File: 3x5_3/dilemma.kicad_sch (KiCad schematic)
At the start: 248 parts, among them J1 USB_C_Receptacle_USB2.0, J102 NA_serial, J105 NA_Conn_01x04_Female, J113 Cirque, J3 NA_GC9A01, J4 Conn_01x05, J5 NA_Conn_01x02, J5001 USB_C_Receptacle_USB2.0, J5002 NA_Conn_01x02, J5003 NA_serial, J5004 NA_GC9A01, J5005 NA_Conn_01x04_Female, J5007 Cirque, J5008 Conn_01x05, J5009 Conn_01x05, J5010 Conn_01x05, SW1 SW_Push, SW101 NA_SW_Push, SW102 NA_SW_Push, SW103 NA_SW_Push, SW104 NA_SW_Push, SW105 NA_SW_Push, SW106 NA_SW_Push, SW107 NA_SW_Push, SW108 NA_SW_Push, SW109 NA_SW_Push, SW112 NA_SW_Push, SW113 NA_SW_Push, SW114 NA_SW_Push, SW115 NA_SW_Push, SW116 NA_SW_Push, SW117 NA_SW_Push, SW118 NA_SW_Push, SW119 NA_SW_Push, SW3001 NA_SW_Push, SW3002 NA_RotaryEncoder_Switch, SW5001 SW_Push, SW5002 NA_SW_Push, SW5003 NA_SW_Push, SW5004 NA_SW_Push, SW5005 NA_SW_Push, SW5006 NA_SW_Push, SW5007 NA_SW_Push, SW5008 NA_SW_Push, SW5009 NA_SW_Push, SW5010 NA_SW_Push, SW5011 NA_SW_Push, SW5012 NA_SW_Push, SW5013 NA_SW_Push, SW5014 NA_SW_Push, SW5015 NA_SW_Push, SW5016 NA_SW_Push, SW5017 NA_SW_Push, SW5018 NA_SW_Push, SW5019 NA_SW_Push, SW5020 NA_RotaryEncoder_Switch, SW5021 SW_SPST, SW5022 SW_SPST, U1 RP2040, U2 W25Q128JVS, U3 XC6210B332MR-G, U4 USBLC6-2P6, U5001 XC6210B332MR-G, U5002 RP2040, U5003 USBLC6-2P6, U5004 W25Q128JVS, U5005 USBLC6-2P6, U5006 USBLC6-2P6, Y1 Crystal_GND24, Y5001 Crystal_GND24

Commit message: add vik connector
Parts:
- added NA_JP5001, NA_JP5002, NA_JP5003, NA_JP5004: NA_Jumper_2_Open, local-libraries:SolderJumper-2_P1.3mm_Open_RoundedPad1.0x1.5mm, symbol Jumper:Jumper_2_Open
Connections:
- net QP_CS is gone; now on net VIK_GP1: J3.6 (~{CS}), U1.15 (GPIO12)
- net QP_CS_L is gone; now on net VIK_GP1_L: J5004.6 (~{CS}), U5002.15 (GPIO12)
- net QP_DC is gone; now on net VIK_GP2: J3.5 (D/C), U1.14 (GPIO11)
- net QP_DC_L is gone; now on net VIK_GP2_L: J5004.5 (D/C), U5002.14 (GPIO11)
- net +5V: now also NA_JP5004.1 (A)
- net +5V_L: now also NA_JP5003.1 (A)
- net at D5033.1 (DOUT): now also NA_JP5002.1 (A)
- net at D5051.1 (DOUT): now also NA_JP5001.1 (A)
- net VIK_GP2_L: now reaches J5007.4 (Pin_4)
- net VIK_GP1_L: now reaches J5007.6 (Pin_6)
- net at J5007.7 (Pin_7): now also NA_JP5003.2 (B)
- net VIK_RGB_L: now reaches J5007.8 (Pin_8)
- net VIK_RGB_L: now also NA_JP5001.2 (B)
- net VIK_GP2: now reaches J113.4 (Pin_4)
- net VIK_GP1: now reaches J113.6 (Pin_6)
- net at J113.7 (Pin_7): now also NA_JP5004.2 (B)
- net VIK_RGB: now reaches J113.8 (Pin_8)
- net VIK_RGB: now also NA_JP5002.2 (B)
- no-connect marks 30 -> 20
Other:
- moved on the sheet: C5001, C5002, C5003, C5004, C5005, C5006, C5007, C5008, C5009, C5010, C5011, C5012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

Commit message: DRC, leds
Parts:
- removed NA_JP5001, NA_JP5002: NA_Jumper_2_Open, local-libraries:SolderJumper-2_P1.3mm_Open_RoundedPad1.0x1.5mm, symbol Jumper:Jumper_2_Open
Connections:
- net VIK_RGB: now also D5033.1 (DOUT)
- net VIK_RGB_L: now also D5051.1 (DOUT)
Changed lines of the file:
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@@
 	(wire
 		(pts
+			(xy 628.65 76.2) (xy 638.81 76.2)
+		)
+		(stroke
+			(width 0)
+			(type default)
+		)
+	)
+	(wire
+		(pts
 			(xy 97.79 106.68) (xy 105.41 106.68)
 		)
@@
 	(wire
 		(pts
+			(xy 622.3 372.11) (xy 632.46 372.11)
+		)
+		(stroke
+			(width 0)
+			(type default)
+		)
+	)
+	(wire
+		(pts
 			(xy 455.93 359.41) (xy 473.71 359.41)
 		)
@@
 	)
 	(symbol
-		(lib_id "Jumper:Jumper_2_Open")
-		(at 633.73 76.2 0)
-		(unit 1)
-		(exclude_from_sim no)
-		(in_bom no)
-		(on_board yes)
-		(dnp no)
-		(property "Reference" "NA_JP5002"
-			(at 632.714 72.898 0)
-			(effects
-				(font
-					(size 1.27 1.27)
-				)
-			)
-		)
-		(property "Value" "NA_Jumper_2_Open"
-			(at 642.112 69.596 0)
-			(effects
-				(font
-					(size 1.27 1.27)
-				)
-			)
-		)
-		(property "Footprint" "local-libraries:SolderJumper-2_P1.3mm_Open_RoundedPad1.0x1.5mm"
-			(at 633.73 76.2 0)
-			(effects
-				(font
-					(size 1.27 1.27)
-				)
-				(hide yes)
-			)
-		)
-		(property "Datasheet" "~"
-			(at 633.73 76.2 0)
-			(effects
-				(font
-					(size 1.27 1.27)
-				)
-				(hide yes)
-			)
-		)
-		(property "Description" ""
-			(at 633.73 76.2 0)
-			(effects
-				(font
-					(size 1.27 1.27)
-				)
-				(hide yes)
-			)
-		)
-		(pin "1"
-		)
-		(pin "2"
-		)
-		(instances
-			(project "dilemma"
-				(path "/7353e96a-343a-4876-b497-b1d205a14d97"
-					(reference "NA_JP5002")
-					(unit 1)
-				)
-			)
-		)
-	)
-	(symbol
 		(lib_id "Switch:SW_Push")
 		(at 129.54 238.76 0)
@@
 					(unit 1)
 				)
-			)
-		)
-	)
-	(symbol
-		(lib_id "Jumper:Jumper_2_Open")
-		(at 627.38 372.11 0)
-		(unit 1)
-		(exclude_from_sim no)
-		(in_bom no)
-		(on_board yes)
-		(dnp no)
-		(property "Reference" "NA_JP5001"
-			(at 626.364 368.808 0)
-			(effects
-				(font
-					(size 1.27 1.27)
-				)
-			)
-		)
-		(property "Value" "NA_Jumper_2_Open"
-			(at 635.762 365.506 0)
-			(effects
-				(font
-					(size 1.27 1.27)
-				)
-			)
-		)
-		(property "Footprint" "local-libraries:SolderJumper-2_P1.3mm_Open_RoundedPad1.0x1.5mm"
-			(at 627.38 372.11 0)
-			(effects
-				(font
-					(size 1.27 1.27)
-				)
-				(hide yes)
-			)
-		)
-		(property "Datasheet" "~"
-			(at 627.38 372.11 0)
-			(effects
-				(font
-					(size 1.27 1.27)
-				)
-				(hide yes)
-			)
-		)
-		(property "Description" ""
-			(at 627.38 372.11 0)
-			(effects
-				(font
-					(size 1.27 1.27)
-				)
-				(hide yes)
-			)
-		)
-		(pin "1"
-		)
-		(pin "2"
-		)
-		(instances
-			(project "dilemma"
-				(path "/7353e96a-343a-4876-b497-b1d205a14d97"
-					(reference "NA_JP5001")
-					(unit 1)
-				)

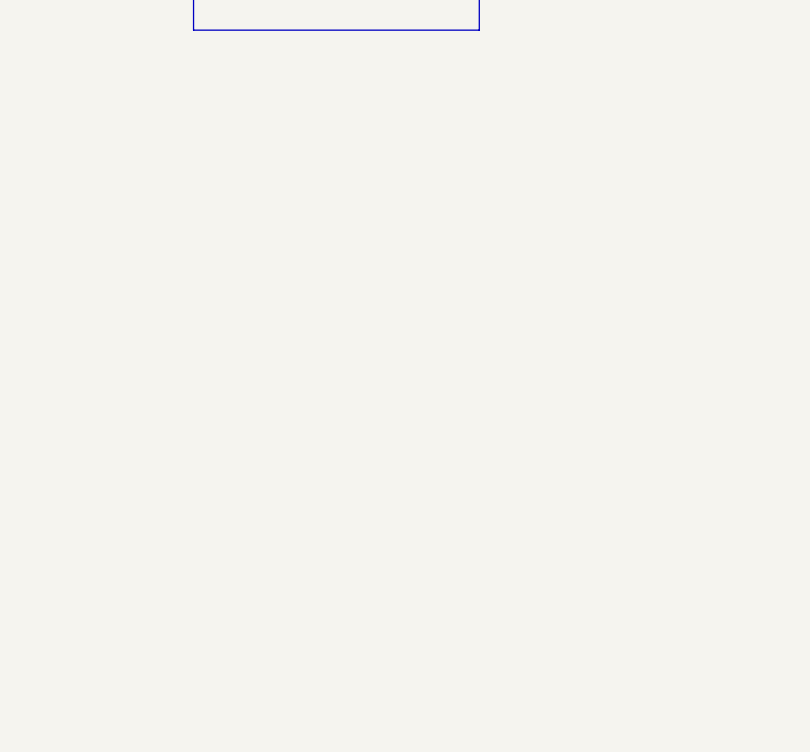
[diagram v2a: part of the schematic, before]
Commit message: NPTH mouse bites
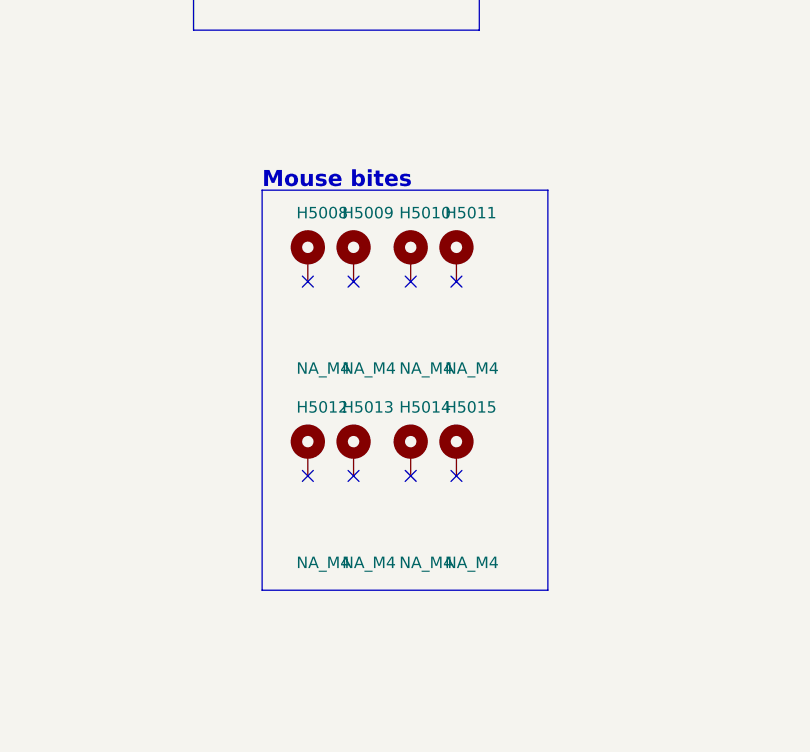
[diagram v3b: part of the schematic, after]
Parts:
- added H5008, H5009, H5010, H5011, H5012, H5013, H5014, H5015: NA_M4, local-libraries:mousebite, symbol Mechanical:MountingHole_Pad
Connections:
- no-connect marks 20 -> 28
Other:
- note added: "Mouse bites"

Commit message: add back non hotswap 3x5_3
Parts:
- removed H5009, H5010, H5011, H5012, H5013, H5014, H5015: NA_M4, local-libraries:mousebite, symbol Mechanical:MountingHole_Pad
- removed NA_JP5003, NA_JP5004: NA_Jumper_2_Open, local-libraries:SolderJumper-2_P1.3mm_Open_RoundedPad1.0x1.5mm, symbol Jumper:Jumper_2_Open
- added H111: NA_Mount, local-libraries:Tenting_Puck, symbol Mechanical:MountingHole_Pad
- H5008: value NA_M4 -> NA_Mount; footprint local-libraries:mousebite -> local-libraries:Tenting_Puck
- J5, J5002: footprint local-libraries:PinHeader_1x02_P1.27mm_Vertical -> Connector_PinHeader_1.27mm:PinHeader_1x02_P1.27mm_Vertical
- SW101, SW102, SW103, SW104, SW105, SW106, SW107, SW108, SW109, SW112, SW113, SW114, SW115, SW116, SW117, SW118, SW119, SW3001, SW5002, SW5003, SW5004, SW5005, SW5006, SW5007, SW5008, SW5009, SW5010, SW5011, SW5012, SW5013, SW5014, SW5015, SW5016, SW5017, SW5018, SW5019: footprint local-libraries:Kailh_socket_PG1350 -> local-libraries:SW_MX_choc
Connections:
- net +3V3: now also J3.2 (GND); no longer J3.1 (VCC)
- net +3V3_L: now also J5004.2 (GND); no longer J5004.1 (VCC)
- net GND: now also J3.1 (VCC), H111.1; no longer J3.2 (GND)
- net GND_L: now also H5008.1, J5004.1 (VCC); no longer J5004.2 (GND)
- net ~{RESET_L}: now also SW5001.2; no longer J5002.2 (Pin_2)
- net ~{RESET}: now also SW1.2; no longer J5.2 (Pin_2)
- net at R5003.1: now also J5002.2 (Pin_2); no longer SW5001.2
- net at R3.1: now also J5.2 (Pin_2); no longer SW1.2
- net VIK_GP1 renamed QP_CS
- net QP_CS: no longer J113.6 (Pin_6)
- net VIK_GP1_L renamed QP_CS_L
- net QP_CS_L: no longer J5007.6 (Pin_6)
- net VIK_GP2 renamed QP_DC
- net QP_DC: no longer J113.4 (Pin_4)
- net VIK_GP2_L renamed QP_DC_L
- net QP_DC_L: no longer J5007.4 (Pin_4)
- net VIK_RGB: no longer names the net of D5033.1 (DOUT)
- net VIK_RGB: no longer J113.8 (Pin_8)
- net VIK_RGB_L: no longer names the net of D5051.1 (DOUT)
- net VIK_RGB_L: no longer J5007.8 (Pin_8)
- no-connect marks 28 -> 30
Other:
- note added: "Tenting puck"
- note removed: "Mouse bites"
- moved on the sheet: C5001, C5002, C5003, C5004, C5005, C5006, C5007, C5008, C5009, C5010, C5011, C5012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

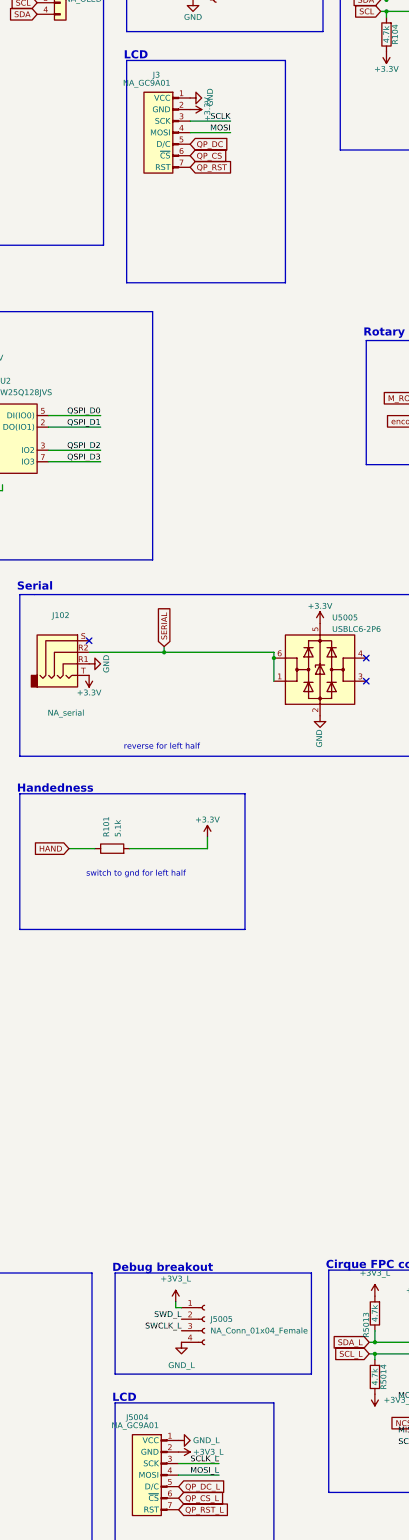
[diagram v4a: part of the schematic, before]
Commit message: fix lcd header
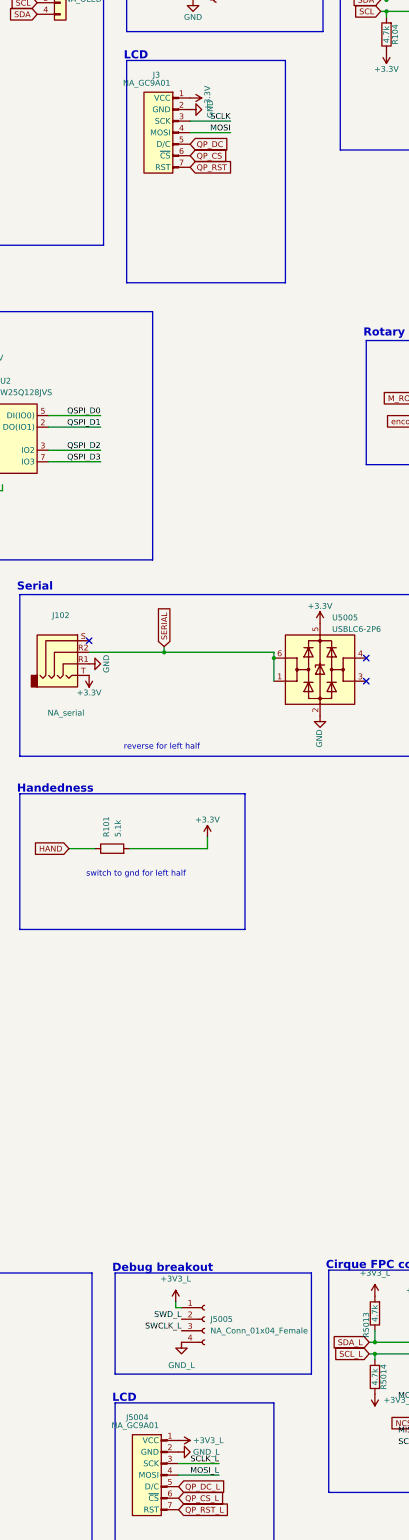
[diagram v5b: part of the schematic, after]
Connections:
- net +3V3: now also J3.1 (VCC); no longer J3.2 (GND)
- net +3V3_L: now also J5004.1 (VCC); no longer J5004.2 (GND)
- net GND: now also J3.2 (GND); no longer J3.1 (VCC)
- net GND_L: now also J5004.2 (GND); no longer J5004.1 (VCC)
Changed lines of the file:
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@@
     )
   )
-  (symbol (lib_id "power_L:+3V3_L") (at 285.115 354.965 270) (unit 1)
+  (symbol (lib_id "power_L:+3V3_L") (at 285.115 352.425 270) (unit 1)
     (in_bom yes) (on_board yes) (dnp no) (fields_autoplaced)
-    (property "Reference" "#PWR05043" (at 281.305 354.965 0)
+    (property "Reference" "#PWR05043" (at 281.305 352.425 0)
       (effects (font (size 1.27 1.27)) hide)
     )
-    (property "Value" "+3V3_L" (at 288.29 354.9649 90)
+    (property "Value" "+3V3_L" (at 288.29 352.4249 90)
       (effects (font (size 1.27 1.27)) (justify left))
     )
-    (property "Footprint" "" (at 285.115 354.965 0)
+    (property "Footprint" "" (at 285.115 352.425 0)
       (effects (font (size 1.27 1.27)) hide)
     )
-    (property "Datasheet" "" (at 285.115 354.965 0)
+    (property "Datasheet" "" (at 285.115 352.425 0)
       (effects (font (size 1.27 1.27)) hide)
     )
@@
     )
   )
-  (symbol (lib_id "power:+3.3V") (at 287.655 59.69 270) (unit 1)
+  (symbol (lib_id "power:+3.3V") (at 287.655 57.15 270) (unit 1)
     (in_bom yes) (on_board yes) (dnp no)
-    (property "Reference" "#PWR0109" (at 283.845 59.69 0)
+    (property "Reference" "#PWR0109" (at 283.845 57.15 0)
       (effects (font (size 1.27 1.27)) hide)
     )
-    (property "Value" "+3.3V" (at 291.465 59.69 0)
+    (property "Value" "+3.3V" (at 291.465 57.15 0)
       (effects (font (size 1.27 1.27)))
     )
-    (property "Footprint" "" (at 287.655 59.69 0)
+    (property "Footprint" "" (at 287.655 57.15 0)
       (effects (font (size 1.27 1.27)) hide)
     )
-    (property "Datasheet" "" (at 287.655 59.69 0)
+    (property "Datasheet" "" (at 287.655 57.15 0)
       (effects (font (size 1.27 1.27)) hide)
     )
@@
     )
   )
-  (symbol (lib_id "power_L:GND_L") (at 285.115 352.425 90) (unit 1)
+  (symbol (lib_id "power_L:GND_L") (at 285.115 354.965 90) (unit 1)
     (in_bom yes) (on_board yes) (dnp no) (fields_autoplaced)
-    (property "Reference" "#PWR05044" (at 291.465 352.425 0)
+    (property "Reference" "#PWR05044" (at 291.465 354.965 0)
       (effects (font (size 1.27 1.27)) hide)
     )
-    (property "Value" "GND_L" (at 288.29 352.4249 90)
+    (property "Value" "GND_L" (at 288.29 354.9649 90)
       (effects (font (size 1.27 1.27)) (justify right))
     )
-    (property "Footprint" "" (at 285.115 352.425 0)
+    (property "Footprint" "" (at 285.115 354.965 0)
       (effects (font (size 1.27 1.27)) hide)
     )
-    (property "Datasheet" "" (at 285.115 352.425 0)
+    (property "Datasheet" "" (at 285.115 354.965 0)
       (effects (font (size 1.27 1.27)) hide)
     )
@@
     )
   )
-  (symbol (lib_id "power:GND") (at 287.655 57.15 90) (unit 1)
+  (symbol (lib_id "power:GND") (at 287.655 59.69 90) (unit 1)
     (in_bom yes) (on_board yes) (dnp no)
-    (property "Reference" "#PWR0106" (at 294.005 57.15 0)
+    (property "Reference" "#PWR0106" (at 294.005 59.69 0)
       (effects (font (size 1.27 1.27)) hide)
     )
-    (property "Value" "GND" (at 292.0492 57.023 0)
+    (property "Value" "GND" (at 292.0492 59.563 0)
       (effects (font (size 1.27 1.27)))
     )
-    (property "Footprint" "" (at 287.655 57.15 0)
+    (property "Footprint" "" (at 287.655 59.69 0)
       (effects (font (size 1.27 1.27)) hide)
     )
-    (property "Datasheet" "" (at 287.655 57.15 0)
+    (property "Datasheet" "" (at 287.655 59.69 0)
       (effects (font (size 1.27 1.27)) hide)
     )

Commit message: change flash header to SMD
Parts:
- J5, J5002: footprint Connector_PinHeader_1.27mm:PinHeader_1x02_P1.27mm_Vertical -> local-libraries:pinheader_1.27mm_1x02_SMD
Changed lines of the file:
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@@
       (effects (font (size 1.27 1.27)) (justify left) hide)
     )
-    (property "Footprint" "Connector_PinHeader_1.27mm:PinHeader_1x02_P1.27mm_Vertical" (at 69.215 174.625 0)
+    (property "Footprint" "local-libraries:pinheader_1.27mm_1x02_SMD" (at 69.215 174.625 0)
       (effects (font (size 1.27 1.27)) hide)
     )
@@
       (effects (font (size 1.27 1.27)) (justify left) hide)
     )
-    (property "Footprint" "Connector_PinHeader_1.27mm:PinHeader_1x02_P1.27mm_Vertical" (at 66.675 469.9 0)
+    (property "Footprint" "local-libraries:pinheader_1.27mm_1x02_SMD" (at 66.675 469.9 0)
       (effects (font (size 1.27 1.27)) hide)
     )

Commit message: routing
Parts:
- SW101, SW102, SW103, SW104, SW105, SW106, SW107, SW108, SW109, SW112, SW113, SW114, SW115, SW116, SW117, SW118, SW119, SW3001, SW5002, SW5003, SW5004, SW5005, SW5006, SW5007, SW5008, SW5009, SW5010, SW5011, SW5012, SW5013, SW5014, SW5015, SW5016, SW5017, SW5018, SW5019: footprint local-libraries:SW_MX_choc -> local-libraries:Kailh_socket_PG1350

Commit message: routing
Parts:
- removed H111, H5008: NA_Mount, local-libraries:Tenting_Puck, symbol Mechanical:MountingHole_Pad
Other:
- note removed: "Tenting puck"
